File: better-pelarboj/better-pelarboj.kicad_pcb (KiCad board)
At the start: 2 copper layers, 56 parts, among them J1 Conn_01x03_Pin, J2 Conn_01x04, J3 Conn_02x01, Q1 AO3400A, Q2 AO3400A, Q3 AO3401A, Q4 AO3400A, SW1 SW_Push, SW2 SW_SPST, U1 XIAO-ESP32-C3-DIP, U2 TP5100_C379389, U3 MT3608, U4 AMS1117-3.3, U5 AP63205WU

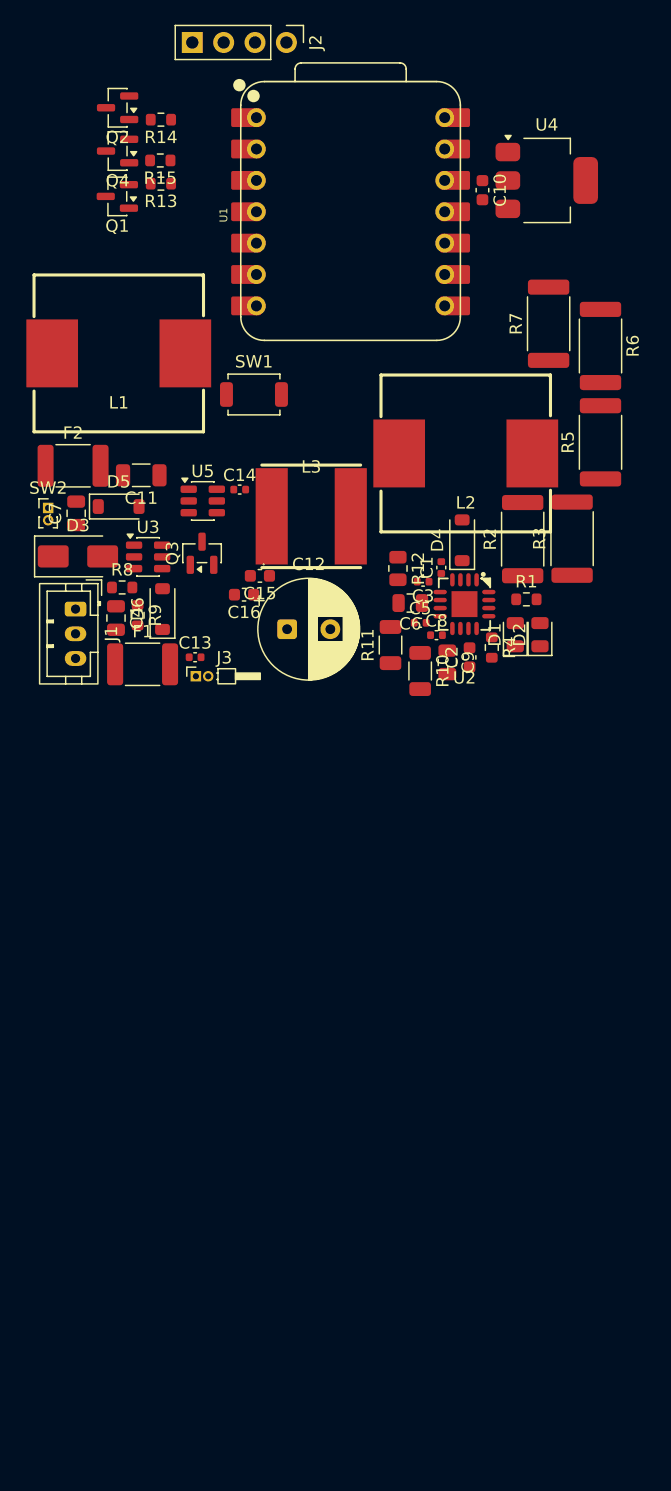
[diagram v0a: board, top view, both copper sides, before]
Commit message: pcb done!!
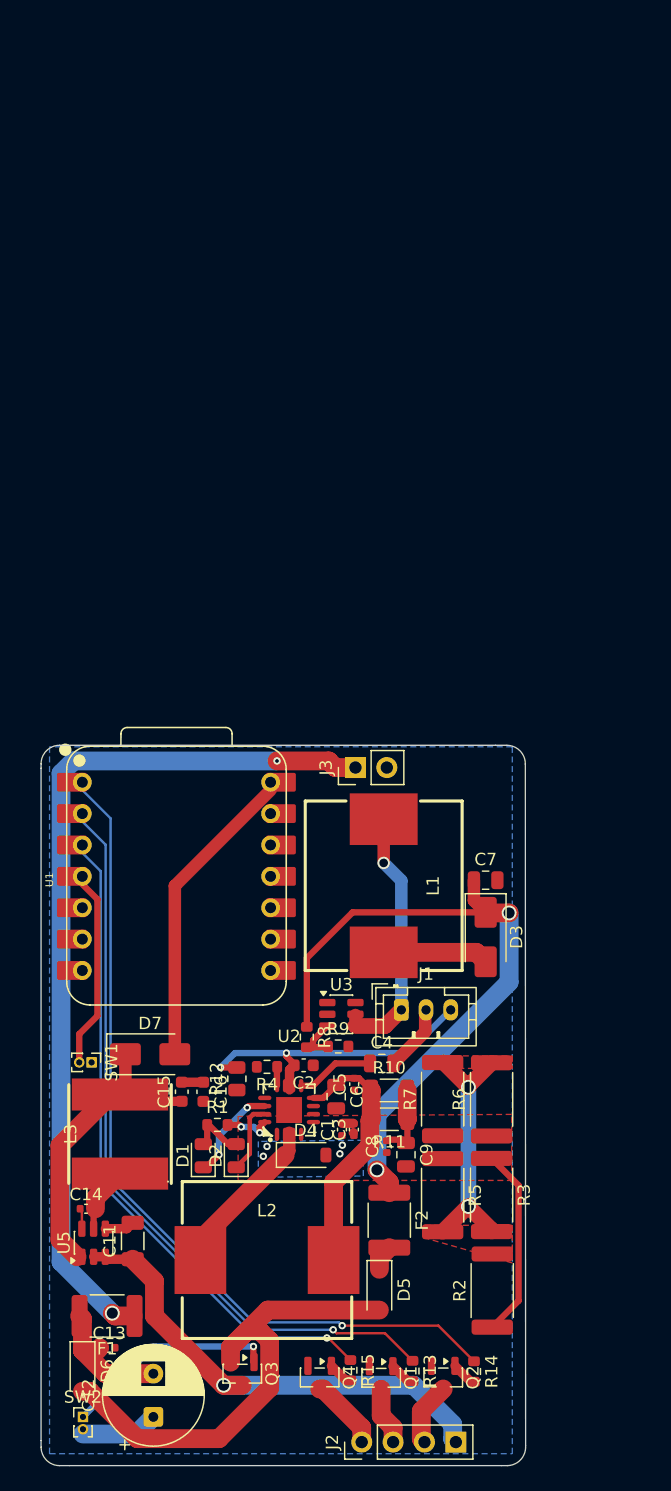
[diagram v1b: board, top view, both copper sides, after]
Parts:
- removed C10: 22u, Capacitor_SMD:C_0603_1608Metric
- removed U4: AMS1117-3.3, Package_TO_SOT_SMD:SOT-223-3_TabPin2
- added D7: D_Schottky, Diode_SMD:D_SMA, F.Cu at (209.4, 118.7)
- J3: footprint Connector_PinHeader_1.00mm:PinHeader_2x01_P1.00mm_Horizontal -> Connector_PinHeader_2.54mm:PinHeader_1x02_P2.54mm_Vertical
- SW1: footprint Button_Switch_SMD:SW_SPST_TS-1088-xR020 -> Connector_PinHeader_1.00mm:PinHeader_1x02_P1.00mm_Vertical
- moved J2 113.5 mm to (226.6, 150.1), turned to 90 degrees
- moved Q2 106.1 mm to (233.2, 144.9), turned to -90 degrees
- moved R14 104.5 mm to (235.7, 144.4), turned to -90 degrees
- moved Q4 100.6 mm to (223.2, 144.9), turned to -90 degrees
- moved R15 99.1 mm to (225.7, 144.3), turned to -90 degrees
- moved R13 98.3 mm to (230.7, 144.4), turned to -90 degrees
- moved Q1 98.0 mm to (228.1, 144.9), turned to -90 degrees
- moved SW2 73.6 mm to (204.0, 148.1)
- moved L2 67.3 mm to (218.9, 135.4), turned to 0 degrees
- moved D5 66.8 mm to (228.0, 137.8), turned to -90 degrees
- moved Q3 66.5 mm to (216.9, 144.6), turned to -90 degrees
- moved F2 66.2 mm to (228.8, 132.2), turned to -90 degrees
- moved C12 64.7 mm to (209.7, 148.1), turned to 90 degrees
- moved R7 63.4 mm to (233.1, 122.4)
- moved R5 62.3 mm to (233.1, 130.1), turned to -90 degrees
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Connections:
- U1 pad 12: +3V3 -> unconnected-(U1-3V3-Pad12)_1
- U1 pad 14: unconnected-(U1-VBUS-Pad14) -> Net-(D7-A)
- U1 pad 2: GREEN_X -> BLUE_X
- U1 pad 3: BLUE_X -> GREEN_X
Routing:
- net Net-(J3-Pin_1): track 0.00 -> 71.7 mm, vias 0 -> 2
- net RED_X: track 0.00 -> 68.0 mm, vias 0 -> 1
- net BLUE_X: track 0.00 -> 60.8 mm, vias 0 -> 1
- net /LiPo_24v: track 0.00 -> 54.0 mm, vias 0 -> 2
- net GREEN_X: track 0.00 -> 53.5 mm, vias 0 -> 1
- net +5V: track 0.00 -> 49.5 mm, vias 0 -> 2
- net Net-(D5-A): track 0.00 -> 40.8 mm
- net +24V: track 0.00 -> 39.4 mm, vias 0 -> 1
- net LiPO+: track 0.00 -> 33.4 mm, vias 0 -> 1
- net LiPO_TS: track 0.00 -> 25.3 mm, vias 0 -> 2
- net Net-(D7-A): track 0.00 -> 24.6 mm
- net Net-(U2-VS): track 0.00 -> 21.5 mm
- net Net-(C1-Pad1): track 0.00 -> 20.2 mm, vias 0 -> 2
- net Net-(Q3-G): track 0.00 -> 17.4 mm, vias 0 -> 1
- net Net-(U1-GPIO5_A3_D3): track 0.00 -> 15.5 mm
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- added copper zone on F.Cu, net +5V
- added copper zone on B.Cu, net GND
- added copper zone on B.Cu, net Net-(C1-Pad1)
- added copper zone on F.Cu, net Net-(C1-Pad1)
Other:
- board outline added: 39.2 x 58.3 mm
